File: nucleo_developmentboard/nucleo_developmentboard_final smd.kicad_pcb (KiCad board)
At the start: 2 copper layers, 65.2 x 82.4 mm, 26 parts, among them J3 Conn_01x02_Socket, J4 MOTOR2 OUT, J5 Conn_PinHeader_1x05_P2.54mm_V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, J6 MOTOR2 OUT, U1 NUCLEO-L432KC, U2 L293D, U3 LM7805_soic, U4 HM-11_Module

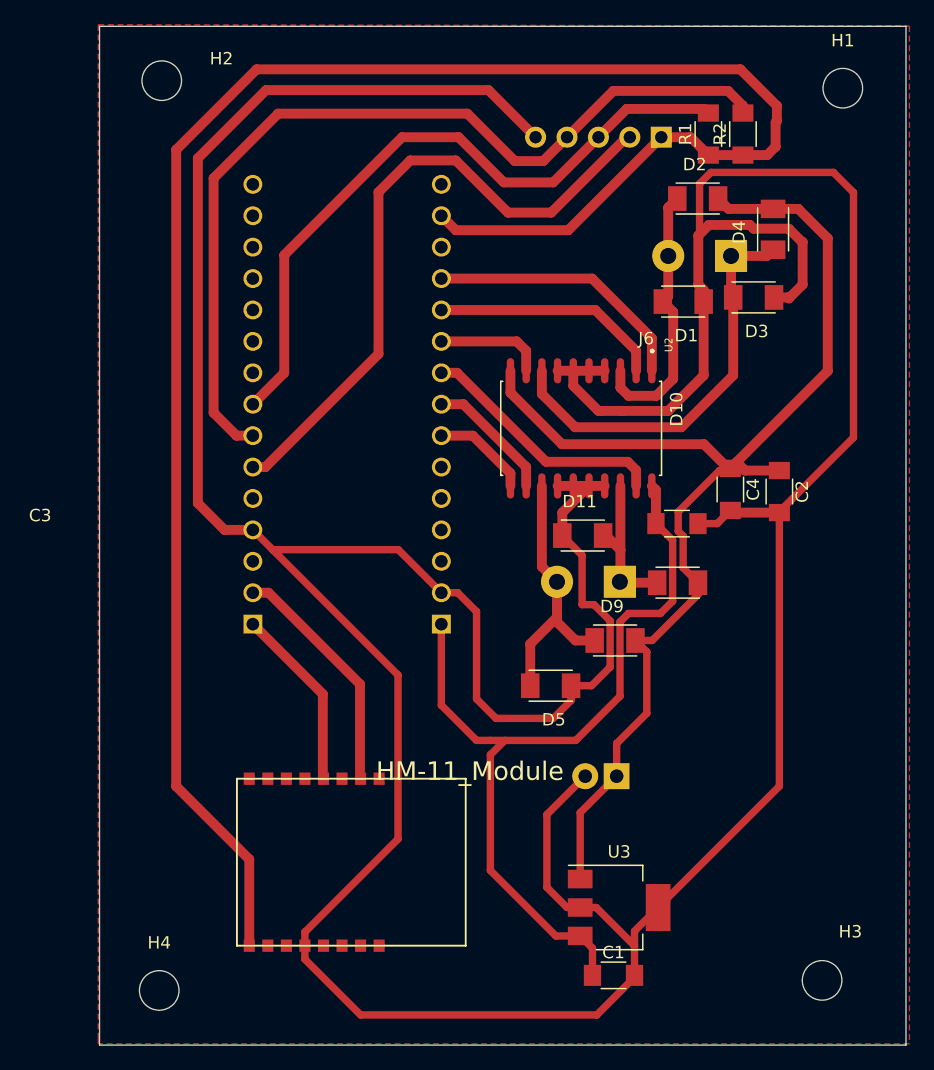
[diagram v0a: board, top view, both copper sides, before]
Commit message: Final Nucleo board updated with all SMD components
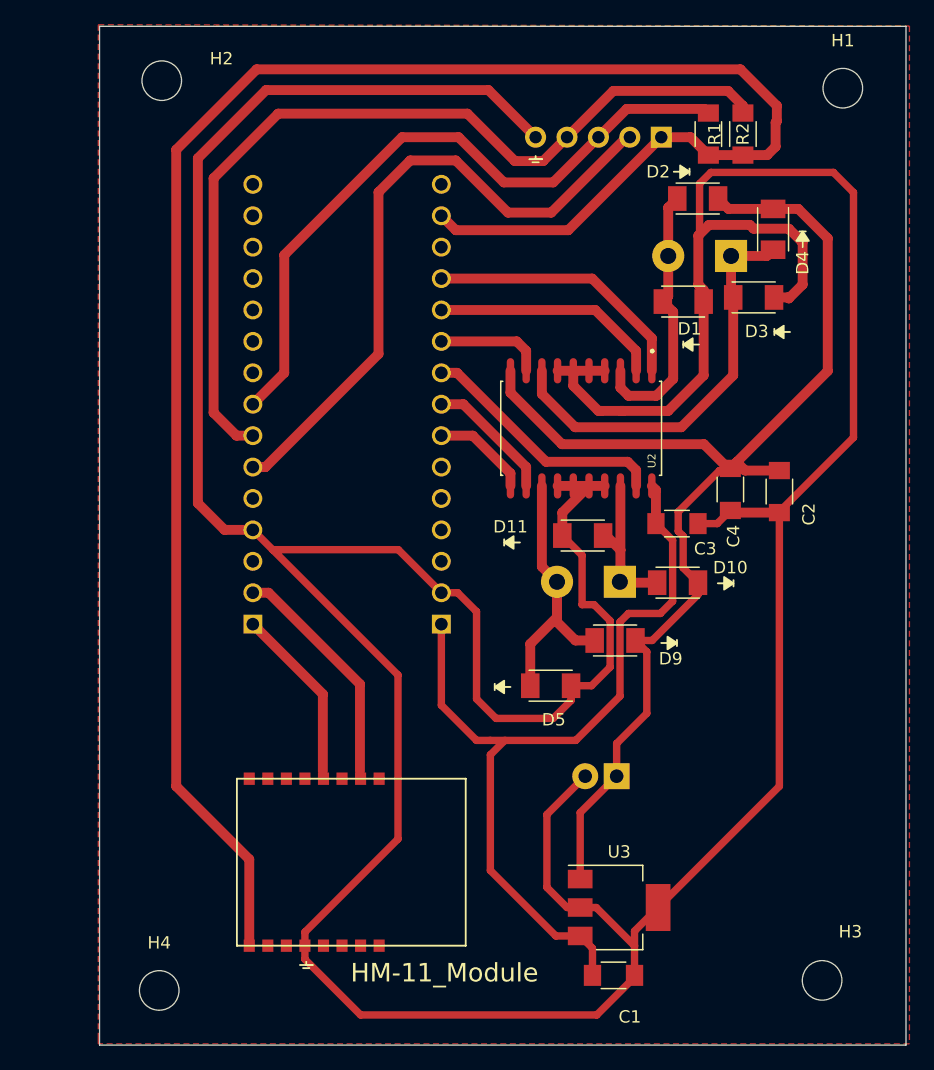
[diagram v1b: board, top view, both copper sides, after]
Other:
- board text added: "CN3_1"
- board text added: "CN4_1"
